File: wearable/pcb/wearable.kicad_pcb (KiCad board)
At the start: 4 copper layers, 28 x 39.2 mm, 82 parts, among them J1 USB_C_Receptacle_USB2.0, J2 Extension, J3 Extension, U1 BC833, U10 TCR3UFxxA, U11 TMP1075, U2 MCP73832-2-OT, U3 S-85S1A, U4 LIS2DE12, U5 APDS-9250, U6 MX25R8035FZxxx0, U7 PCF85063ATL, U8 DT1446-04V, U9 MAX30102, Y71 32.768kHz

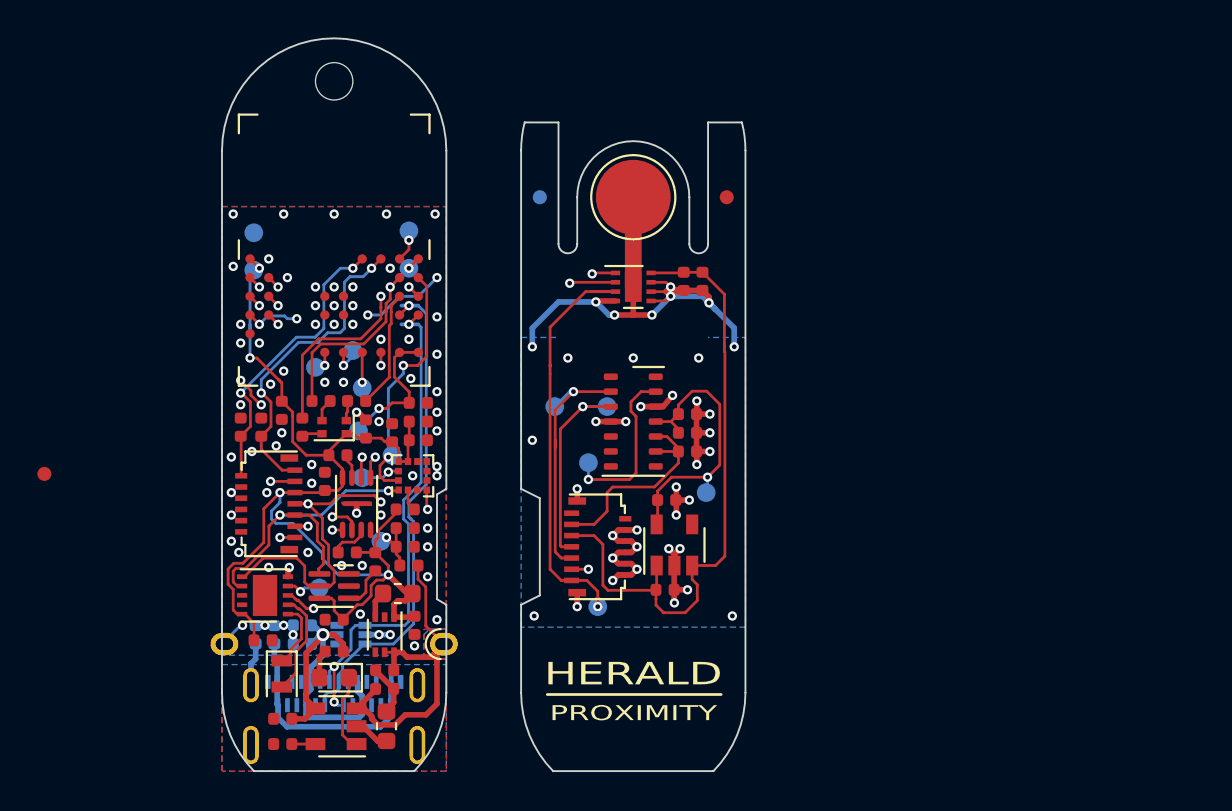
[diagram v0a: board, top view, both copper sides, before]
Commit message: Part of #16. Added GNSS PCB layout
Also added custom footprint for NN02-224 chip antenna.
Signed-off-by: Adam Fowler <adam@adamfowler.org>
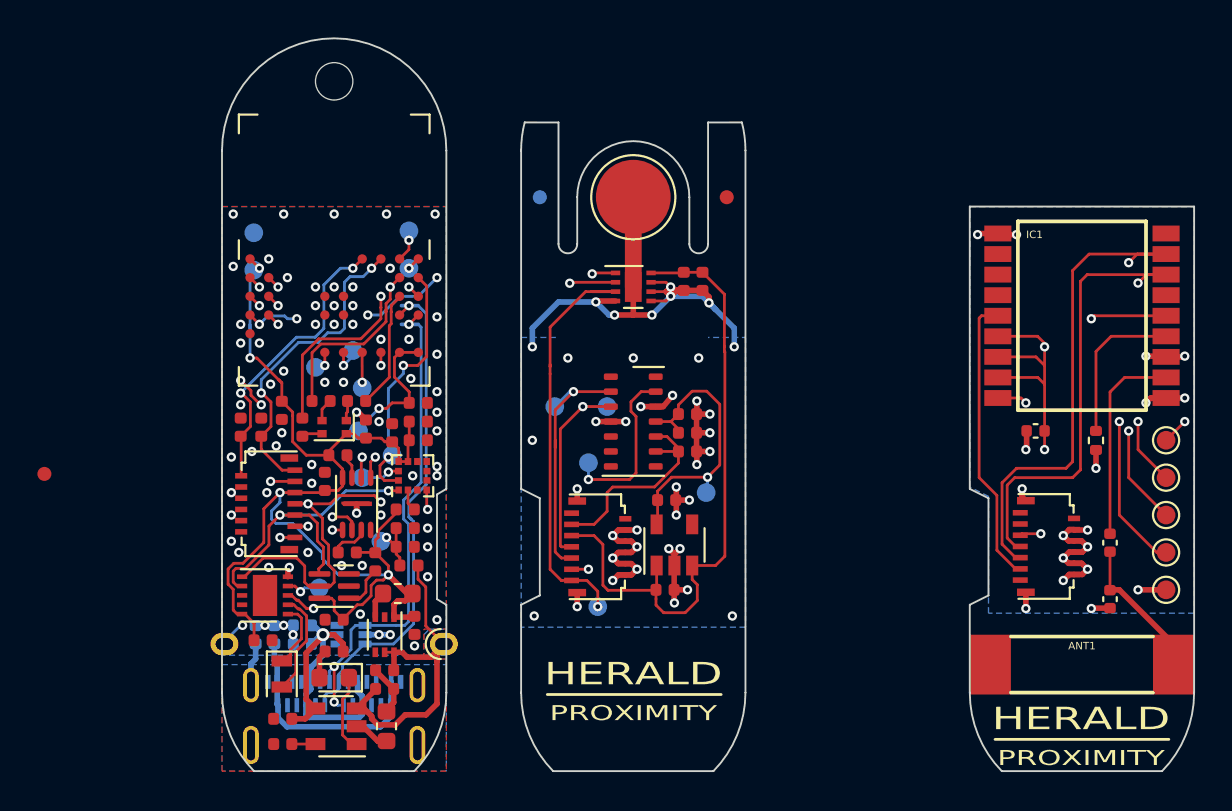
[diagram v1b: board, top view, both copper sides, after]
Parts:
- added ANT1: ~, Herald_Extras:NN02-224, F.Cu at (190.0, 113.0)
- added C4: 120pF, Capacitor_SMD:C_0402_1005Metric, F.Cu at (191.5, 106.5)
- added C5: Tune (~120pF), Capacitor_SMD:C_0402_1005Metric, F.Cu at (191.5, 109.5)
- added C7: 56pF, Capacitor_SMD:C_0402_1005Metric, F.Cu at (187.5, 100.5)
- added IC1: TESEO-LIV3F, Herald_Extras:SON110P970X1010X230-18N, F.Cu at (190.0, 94.3)
- added J4: Extension, Herald_Extras:TE_1-2328724-3_2Rows_13Pins_P0.3mm_Horizontal, F.Cu at (188.8, 106.7)
- added R5: 10k, Resistor_SMD:R_0402_1005Metric, F.Cu at (190.8, 101.0)
- added TP3: VDD1, TestPoint:TestPoint_Pad_D1.0mm, F.Cu at (194.5, 101.0)
- added TP4: SDA, TestPoint:TestPoint_Pad_D1.0mm, F.Cu at (194.5, 103.0)
- added TP7: SCL, TestPoint:TestPoint_Pad_D1.0mm, F.Cu at (194.5, 105.0)
- added TP8: GNSS_RESETn, TestPoint:TestPoint_Pad_D1.0mm, F.Cu at (194.5, 107.0)
- added TP9: GND1, TestPoint:TestPoint_Pad_D1.0mm, F.Cu at (194.5, 109.0)
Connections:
- C93 pad 1: Vdrive -> +1V8
- J1 pad A5: Net-(J1-PadA5) -> unconnected-(J1-CC1-PadA5)
- J1 pad A8: Net-(J1-PadA8) -> unconnected-(J1-SBU1-PadA8)
- J1 pad B5: Net-(J1-PadB5) -> unconnected-(J1-CC2-PadB5)
- J1 pad B8: Net-(J1-PadB8) -> unconnected-(J1-SBU2-PadB8)
- J2 pad 1: /Core Board/TMP_INT -> /Core Board/EXT_INT2
- J2 pad 3: /Core Board/BIO_INT -> /Core Board/EXT_INT1
- J3 pad 1: Net-(J3-Pad1) -> unconnected-(J3-Pin_1-Pad1)
- J3 pad 11: /Extension Board/BIO_INT -> /Core Board/EXT_INT1
- J3 pad 13: /Extension Board/TMP_INT -> /Core Board/EXT_INT2
- J3 pad 2: Net-(J3-Pad2) -> unconnected-(J3-Pin_2-Pad2)
- J3 pad 3: Vdrive -> +1V8
- J3 pad 7: /Extension Board/SDA -> /Core Board/SDA
- J3 pad 9: /Extension Board/SCL -> /Core Board/SCL
- TP111 pad 1: /Extension Board/TMP_INT -> /Core Board/EXT_INT2
- TP5 pad 1: /Extension Board/SCL -> /Core Board/SCL
- TP6 pad 1: /Extension Board/SDA -> /Core Board/SDA
- TP91 pad 1: /Extension Board/BIO_INT -> /Core Board/EXT_INT1
- U1 pad 2: /Core Board/BIO_INT -> /Core Board/EXT_INT1
- U10 pad 4: Net-(U10-Pad4) -> unconnected-(U10-NC-Pad4)
- U11 pad 1: /Extension Board/SDA -> /Core Board/SDA
- U11 pad 2: /Extension Board/SCL -> /Core Board/SCL
- U11 pad 3: /Extension Board/TMP_INT -> /Core Board/EXT_INT2
- U4 pad 3: Net-(U4-Pad3) -> unconnected-(U4-SA0/SDO-Pad3)
- U5 pad 5: Net-(U5-Pad5) -> unconnected-(U5-NC-Pad5)
- U7 pad 8: Net-(U7-Pad8) -> unconnected-(U7-NC-Pad8)
- U7 pad 9: Net-(U7-Pad9) -> unconnected-(U7-CLKO-Pad9)
- U7 pad EP: Net-(U7-PadEP) -> unconnected-(U7-PadEP)
- U8 pad 4: Net-(U8-Pad4) -> unconnected-(U8-Pad4)
- U8 pad 6: Net-(U8-Pad6) -> unconnected-(U8-Pad6)
- U9 pad 1: Net-(U9-Pad1) -> unconnected-(U9-NC-Pad1)
- U9 pad 10: Vdrive -> +1V8
- U9 pad 13: /Extension Board/BIO_INT -> /Core Board/EXT_INT1
- U9 pad 14: Net-(U9-Pad14) -> unconnected-(U9-NC-Pad14)
- U9 pad 2: /Extension Board/SCL -> /Core Board/SCL
- U9 pad 3: /Extension Board/SDA -> /Core Board/SDA
- U9 pad 5: Net-(U9-Pad5) -> unconnected-(U9-NC-Pad5)
- U9 pad 6: Net-(U9-Pad6) -> unconnected-(U9-NC-Pad6)
- U9 pad 7: Net-(U9-Pad7) -> unconnected-(U9-NC-Pad7)
- U9 pad 8: Net-(U9-Pad8) -> unconnected-(U9-NC-Pad8)
- U9 pad 9: Vdrive -> +1V8
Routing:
- net /Core Board/SCL: track 25.8 -> 89.9 mm, vias 3 -> 7
- net /Core Board/SDA: track 31.0 -> 88.4 mm, vias 4 -> 8
- net /Core Board/EXT_INT1: track 0.00 -> 45.6 mm, vias 0 -> 4
- net VDD1: track 34.2 -> 70.5 mm, vias 0 -> 5
- net /Core Board/EXT_INT2: track 0.00 -> 23.3 mm, vias 0 -> 2
- net /Extension Board/SCL: track 23.2 -> 0.00 mm, vias 2 -> 0
- net /Extension Board/TMP_INT: track 22.5 -> 0.00 mm, vias 1 -> 0
- net /Extension Board/SDA: track 21.9 -> 0.00 mm, vias 2 -> 0
- net GND1: track 55.2 -> 75.3 mm, vias 38 -> 56
- net /GNSS Board/GNSS_RESETn: track 0.00 -> 15.4 mm, vias 0 -> 2
- net /Core Board/BIO_INT: track 15.3 -> 0.00 mm, vias 2 -> 0
- net /Extension Board/BIO_INT: track 14.8 -> 0.00 mm, vias 2 -> 0
- net Vdrive: track 11.1 -> 0.00 mm
- net +1V8: track 15.2 -> 26.4 mm
- net /GNSS Board/ANT_RF: track 0.00 -> 11.0 mm
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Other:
- board size 28 x 39.2 mm -> 52 x 39.2 mm
- net class Default removed
- net class GNDPWR removed

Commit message: Part of #16. Corrected antenna placement
Ensured minimum 2.5mm ground plane clearance
Added all component 3D models
Signed-off-by: Adam Fowler <adam@adamfowler.org>
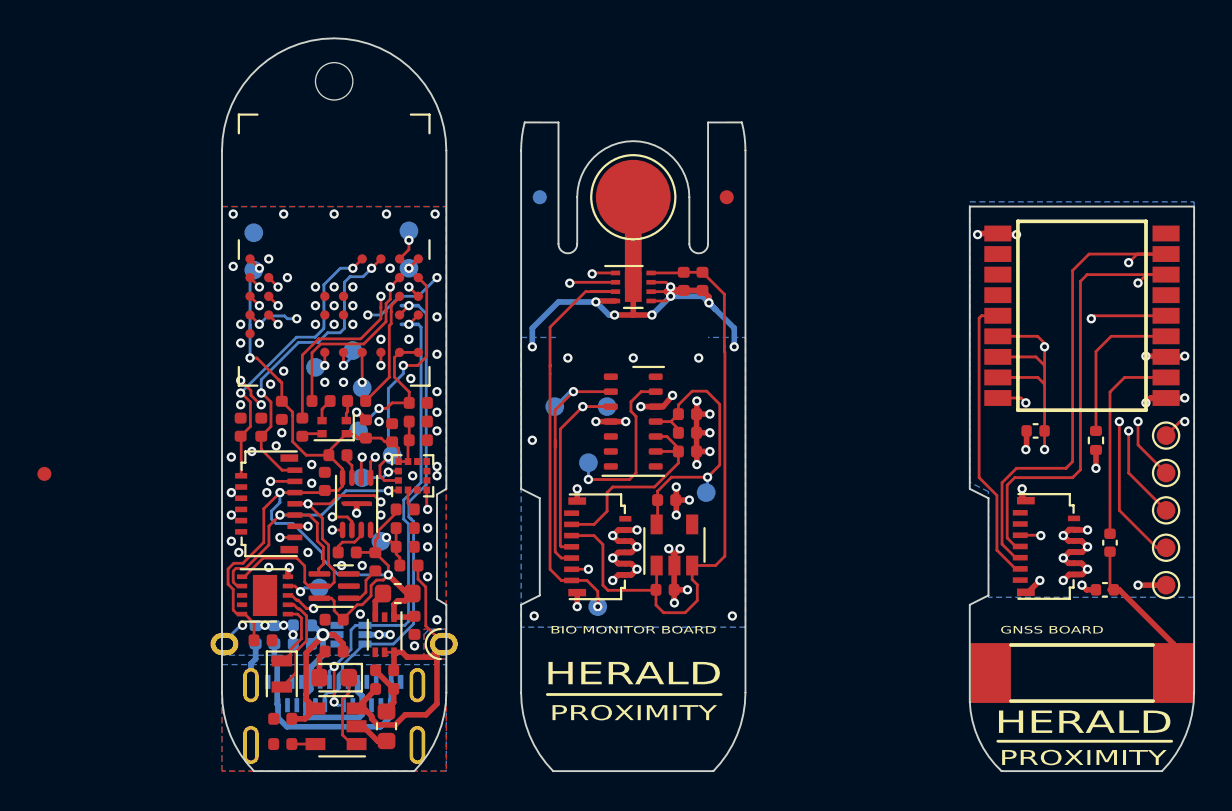
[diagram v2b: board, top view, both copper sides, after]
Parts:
- moved C5 0.57 mm to (191.2, 109.0), turned to 180 degrees
- moved ANT1 0.45 mm to (190.0, 113.5)
- moved TP3 0.25 mm to (194.5, 100.8)
- moved TP4 0.25 mm to (194.5, 102.8)
- moved TP7 0.25 mm to (194.5, 104.8)
- moved TP8 0.25 mm to (194.5, 106.8)
- moved TP9 0.25 mm to (194.5, 108.8)
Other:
- outline, holes or cut-outs redrawn
- board text added: "BIO MONITOR BOARD"
- board text added: "GNSS BOARD"
